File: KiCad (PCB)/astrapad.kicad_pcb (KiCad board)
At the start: 2 copper layers, 99.9 x 53.6 mm, 34 parts, among them J1 OLED_DISPLAY, SW1 SW_Push, SW13 RotaryEncoder_Switch, SW2 SW_Push, SW3 SW_Push, SW5 SW_Push, SW6 SW_Push, SW7 SW_Push, SW8 SW_Push, U1 XIAO-RP2040-DIP

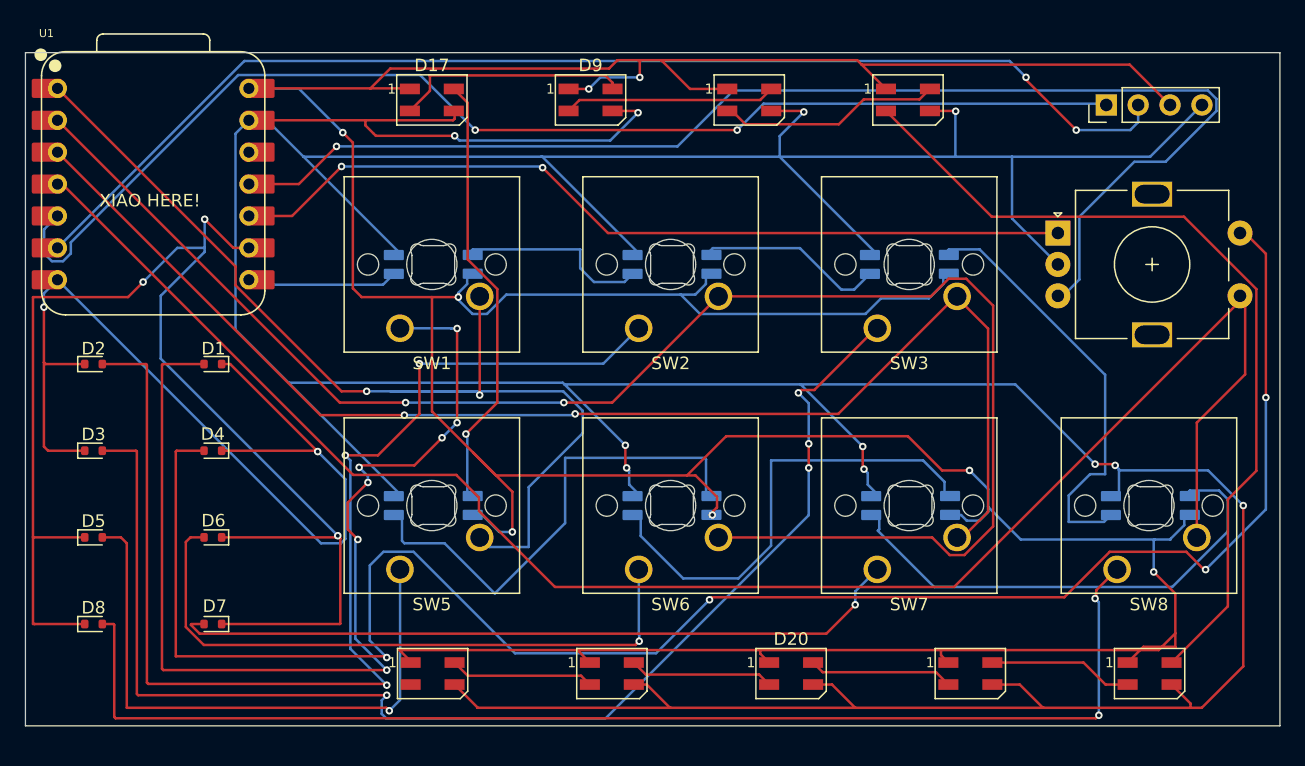
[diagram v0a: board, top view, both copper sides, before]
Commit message: Repositioned Key Backlight LEDS
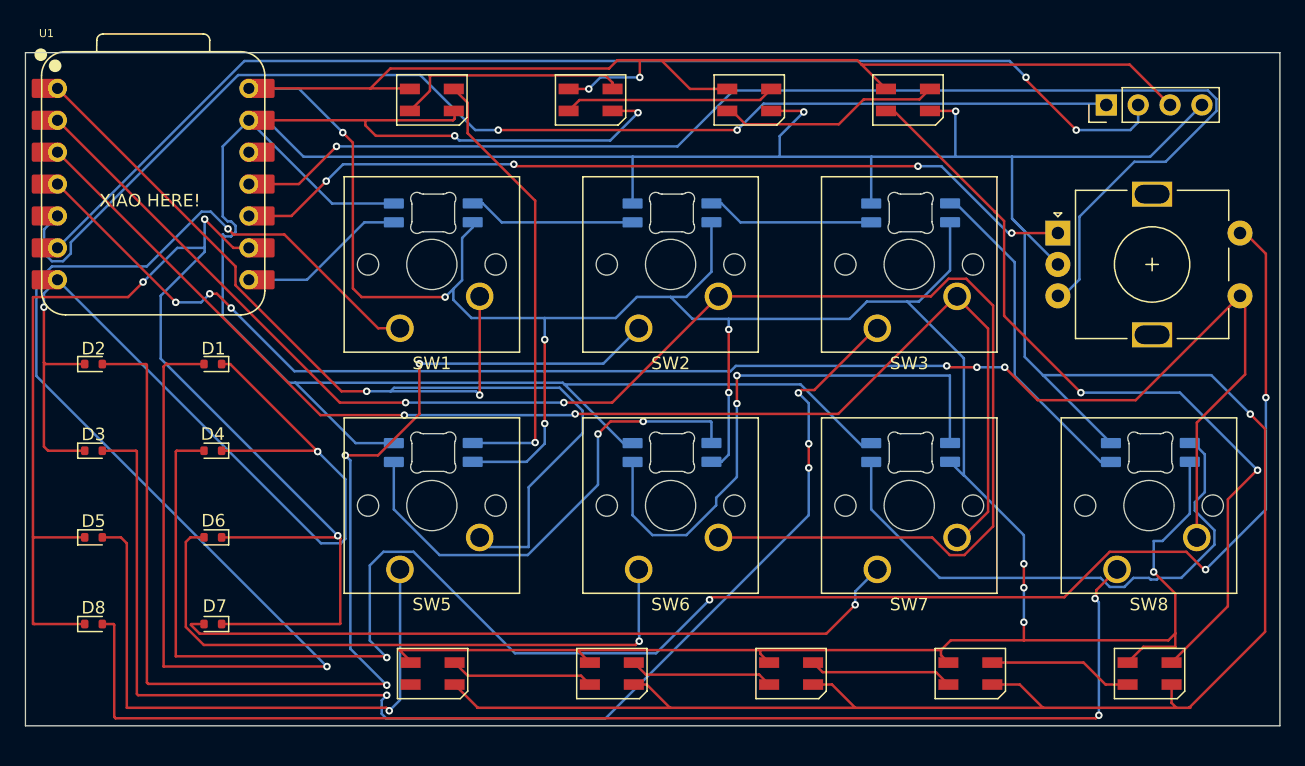
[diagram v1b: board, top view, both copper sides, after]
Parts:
- J1: value OLED_DISPLAY -> Astras_Glasses
- moved D13 4.22 mm to (89.6, 31.8)
- moved D14 4.22 mm to (70.5, 31.8)
- moved D15 4.22 mm to (51.5, 31.8)
- moved D16 4.22 mm to (32.5, 31.8)
- moved D12 4.10 mm to (70.5, 12.8)
- moved D10 4.10 mm to (32.5, 12.8)
- moved D11 4.10 mm to (51.5, 12.8)
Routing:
- net Net-(D1-A): track 85.3 -> 115.5 mm, vias 7 -> 2
- net GND: track 410.6 -> 394.7 mm, vias 11 -> 5
- net +5V: track 352.5 -> 336.8 mm, vias 8 -> 12
- net Column 4: track 139.8 -> 126.5 mm, vias 0 -> 6
- net Net-(D14-DOUT): track 37.0 -> 45.9 mm, vias 0 -> 2
- net Net-(D12-DOUT): track 34.4 -> 26.6 mm
- net Net-(D13-DOUT): track 39.4 -> 44.9 mm
- net Net-(D19-DOUT): track 67.9 -> 64.2 mm, vias 0 -> 2
- net Net-(D10-DOUT): track 15.6 -> 13.4 mm
- net Net-(D11-DOUT): track 15.2 -> 13.3 mm
- net Net-(D10-DIN): track 12.1 -> 13.4 mm
- net Net-(D16-DOUT): track 34.9 -> 35.8 mm
- net Net-(D15-DOUT): track 38.5 -> 39.0 mm, vias 0 -> 2
- net Rotary A: track 67.8 -> 67.6 mm, vias 2 -> 4

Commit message: Some PCB Rerouting And by "some", I mean all of it. I didn't account for the size of the actual OLED screen (just had the pins before), so I had to reroute basically everything once I did.
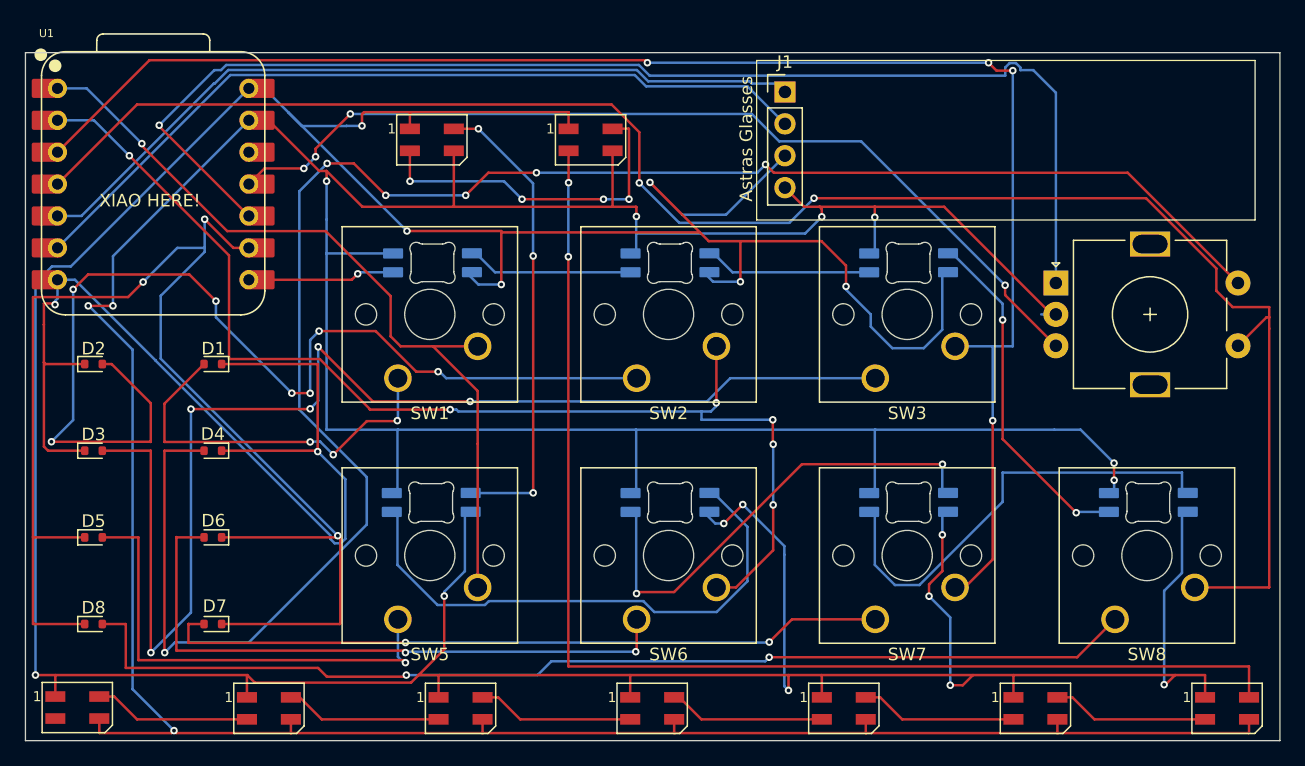
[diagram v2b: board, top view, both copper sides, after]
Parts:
- J1: value Astras_Glasses -> Astras Glasses
- moved D19 81.9 mm to (4.13, 52.1)
- moved D18 61.7 mm to (19.4, 52.2)
- moved D20 34.8 mm to (95.7, 52.2)
- moved J1 25.6 mm to (60.5, 3.13), turned to 0 degrees
- moved D23 10.5 mm to (65.2, 52.2)
- moved D22 9.50 mm to (80.4, 52.2)
- moved D24 4.24 mm to (49.9, 52.2)
- moved SW1 3.98 mm to (29.7, 25.9)
- moved SW2 3.98 mm to (48.7, 25.9)
- moved SW3 3.98 mm to (67.7, 25.9)
- moved D11 3.98 mm to (51.3, 16.7)
- moved D12 3.98 mm to (70.3, 16.7)
- moved D13 3.98 mm to (89.4, 35.8)
- moved D15 3.98 mm to (51.3, 35.8)
- moved D16 3.98 mm to (32.3, 35.8)
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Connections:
- D19 pad 2: Net-(D19-DOUT) -> unconnected-(D19-DOUT-Pad2)
- D22 pad 4: Net-(D19-DOUT) -> Net-(D20-DOUT)
- D23 pad 2: Net-(D20-DIN) -> Net-(D23-DOUT)
- D24 pad 4: Net-(D20-DOUT) -> Net-(D23-DOUT)
- D25 pad 2: unconnected-(D25-DOUT-Pad2) -> Net-(D18-DIN)
- D9 pad 2: Net-(D18-DIN) -> Net-(D20-DIN)
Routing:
- net Net-(D20-DIN): track 11.5 -> 97.7 mm, vias 0 -> 2
- net Net-(D1-A): track 115.5 -> 31.0 mm, vias 2 -> 3
- net Net-(D19-DOUT): track 64.2 -> 0.00 mm, vias 2 -> 0
- net GND: track 394.7 -> 358.5 mm, vias 5 -> 9
- net Column 2: track 129.7 -> 94.3 mm, vias 2 -> 6
- net SDA: track 97.6 -> 63.5 mm, vias 2 -> 0
- net Rotary A: track 67.6 -> 101.0 mm, vias 4 -> 1
- net SCL: track 96.2 -> 65.2 mm, vias 2 -> 0
- net Rotary B: track 101.8 -> 75.0 mm, vias 1 -> 4
- net +5V: track 336.8 -> 359.8 mm, vias 12 -> 15
- net Column 3: track 105.7 -> 126.9 mm, vias 2 -> 4
- net Column 1: track 85.5 -> 64.6 mm, vias 2 -> 1
- net Column 4: track 126.5 -> 142.5 mm, vias 6 -> 2
- net Net-(D8-A): track 99.3 -> 86.3 mm
- net Net-(D2-A): track 97.6 -> 85.1 mm, vias 3 -> 7
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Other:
- board size 99.9 x 53.6 mm -> 99.9 x 54.8 mm
